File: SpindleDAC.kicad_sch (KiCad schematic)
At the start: 8 parts, among them J13 0-10V Spindle Out, U24 ${SIM.PARAMS}, U25 ${SIM.PARAMS}

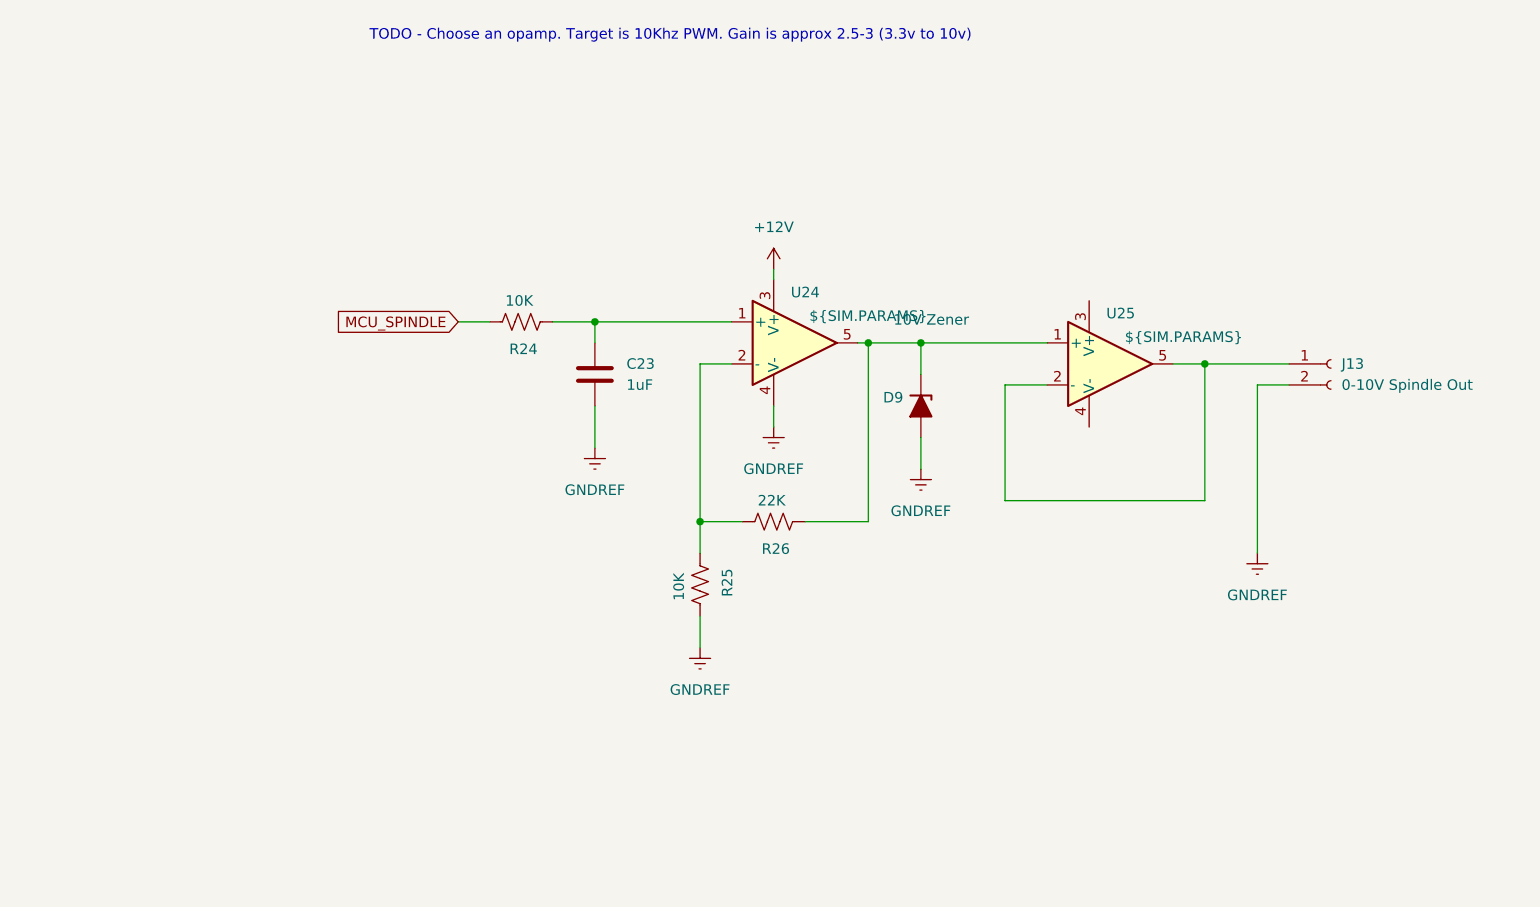
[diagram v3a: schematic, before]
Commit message: restructured power supplies to enable Spindle DAC to be isolated. We now have the option of supplying two 24V inputs, one to power the nucleo and everything logic side and the other to power peripherals. Some testing will be required.
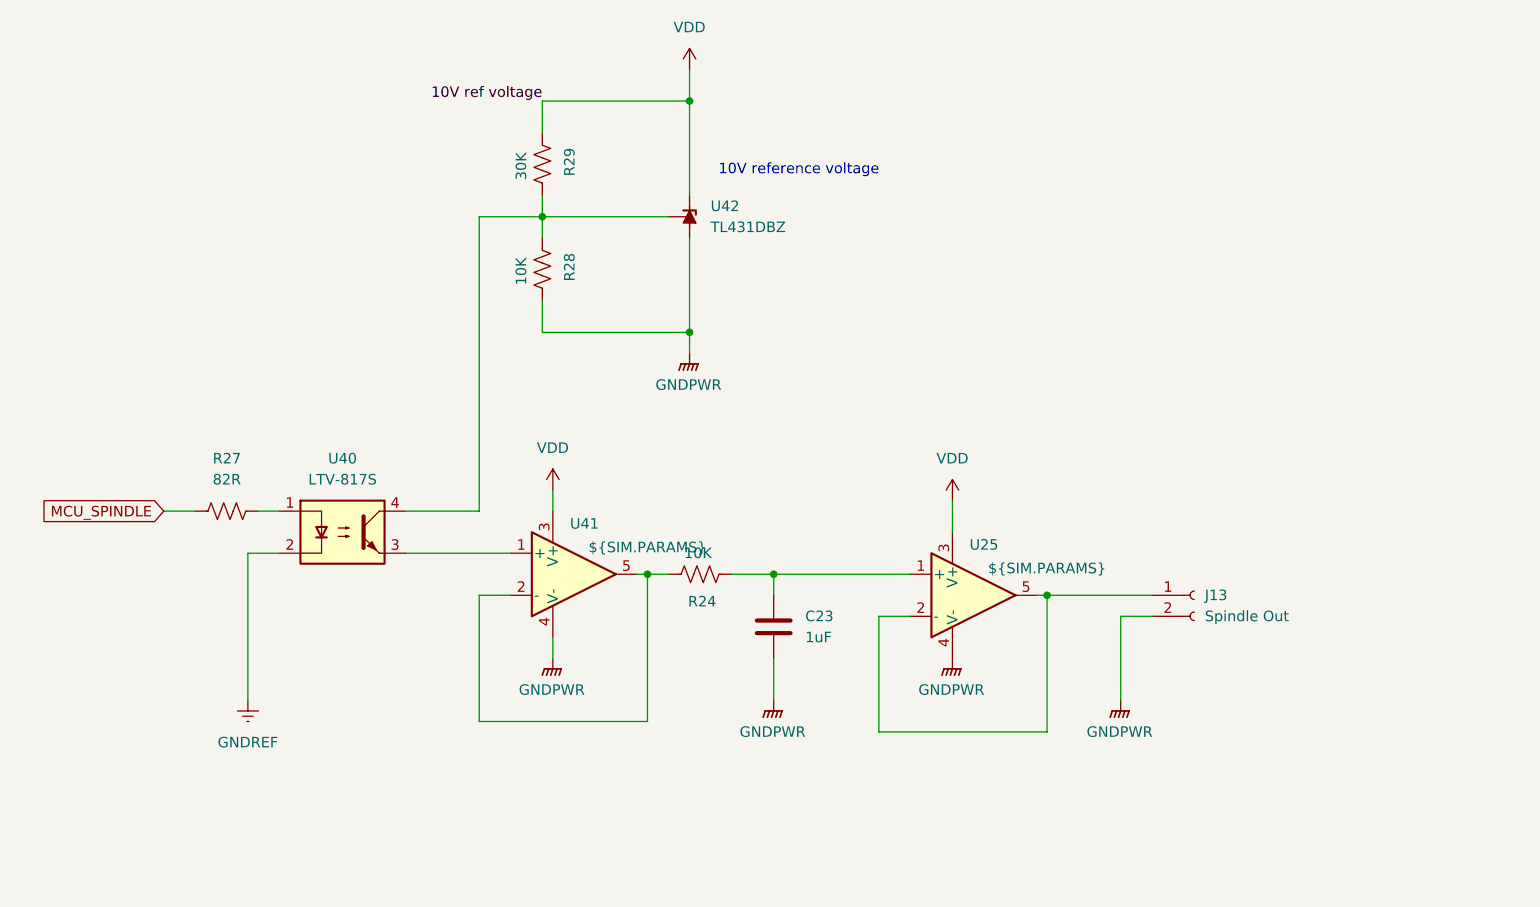
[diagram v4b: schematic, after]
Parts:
- removed D9: 10V Zener, symbol Device:D_Zener_Filled
- removed R25: 10K, symbol Device:R_US
- removed R26: 22K, symbol Device:R_US
- removed U24: ${SIM.PARAMS}, symbol Simulation_SPICE:OPAMP
- added R27: 82R, symbol Device:R_US
- added R28: 10K, symbol Device:R_US
- added R29: 30K, symbol Device:R_US
- added U40: LTV-817S, Package_SO:SOIC-16_3.9x9.9mm_P1.27mm, symbol Isolator:LTV-817S
- added U41: ${SIM.PARAMS}, symbol Simulation_SPICE:OPAMP
- added U42: TL431DBZ, Package_TO_SOT_SMD:SOT-23, symbol Reference_Voltage:TL431DBZ
- J13: value 0-10V Spindle Out -> Spindle Out
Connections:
- net GNDREF: now also U40.2; no longer C23.2, J13.2 (Pin_2)
- net MCU_SPINDLE: now also R27.1; no longer R24.2
- net at U25.1 (+): now also C23.1, R24.1
- net VDD: now reaches U25.3 (V+)
- net VDD: now also R29.1, U41.3 (V+), U42.1 (K)
- net GNDPWR: now reaches U25.4 (V-)
- net GNDPWR: now also C23.2, J13.2 (Pin_2), R28.2, U41.4 (V-), U42.3 (A)
- new net: R28.1, R29.2, U40.4, U42.2 (REF)
- new net: R27.2, U40.1
- new net: U40.3, U41.1 (+)
- new net: R24.2, U41.2 (-), U41.5
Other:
- note added: "10V reference voltage"
- note removed: "TODO - Choose an opamp. Target is 10Khz PWM. Gain is approx 2.5-3 (3.3v to 10v)"
- moved on the sheet: C23, J13, R24, U25

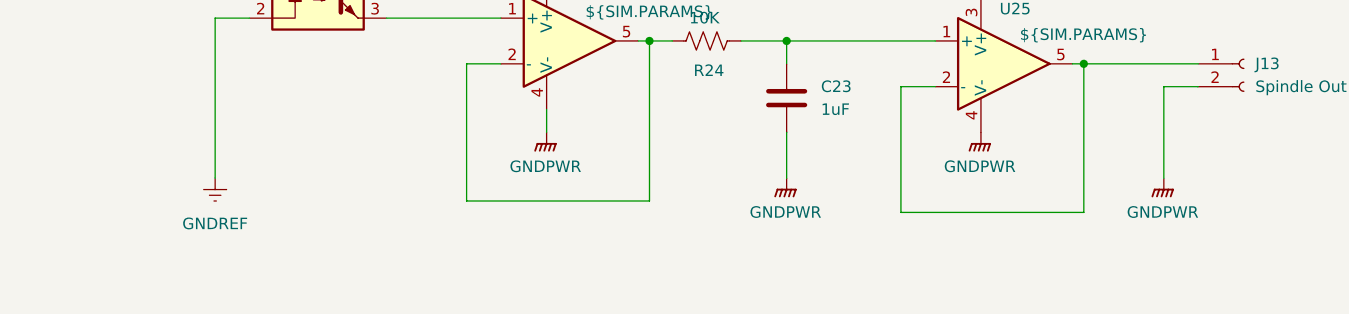
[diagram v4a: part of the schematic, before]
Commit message: Fixes to screw terminal footprints, updated BOM and included in project folder
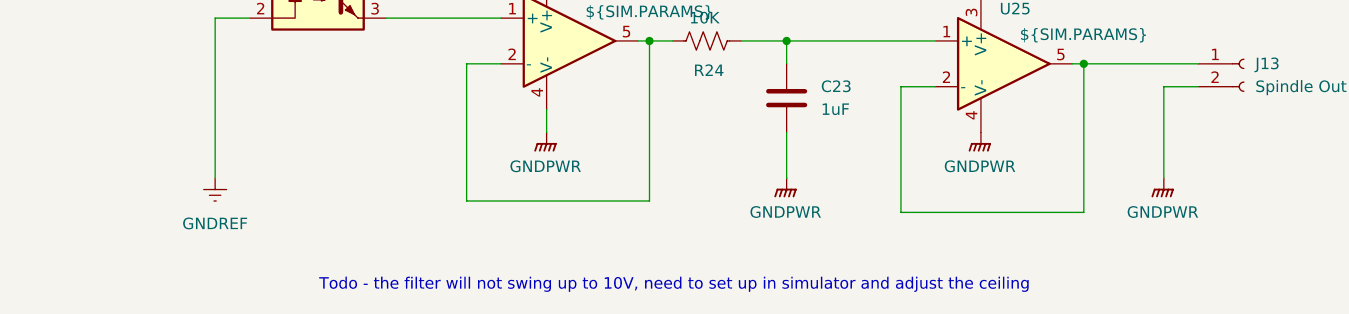
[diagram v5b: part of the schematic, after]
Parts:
- J13: footprint OSTVTerminalBlocks:Conn01x02 -> EBWA_02_A:ADAMTECH_EBWA-02-A
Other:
- note added: "Todo - the filter will not swing up to 10V, need to set up in simulator and adjust the ceiling"
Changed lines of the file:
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@@
+		)
+	)
+	(text "Todo - the filter will not swing up to 10V, need to set up in simulator and adjust the ceiling"
+		(exclude_from_sim no)
+		(at 119.634 128.778 0)
+		(effects
+			(font
+				(size 1.27 1.27)
+			)
 		)
 	)
@@
 			)
 		)
-		(property "Footprint" "OSTVTerminalBlocks:Conn01x02"
+		(property "Footprint" "EBWA_02_A:ADAMTECH_EBWA-02-A"
 			(at 182.88 104.14 0)
 			(effects

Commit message: Fixed bug with lack of pin header for CN11 and CN12. Addeded RPI header and aligned it, assigned some safe footprints
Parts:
- R24, R27, R28, R29: footprint (none) -> Resistor_SMD:R_1206_3216Metric_Pad1.30x1.75mm_HandSolder
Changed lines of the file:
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@@
 			)
 		)
-		(property "Footprint" ""
+		(property "Footprint" "Resistor_SMD:R_1206_3216Metric_Pad1.30x1.75mm_HandSolder"
 			(at 105.156 65.024 90)
 			(effects
@@
 			)
 		)
-		(property "Footprint" ""
+		(property "Footprint" "Resistor_SMD:R_1206_3216Metric_Pad1.30x1.75mm_HandSolder"
 			(at 66.294 92.964 90)
 			(effects
@@
 			)
 		)
-		(property "Footprint" ""
+		(property "Footprint" "Resistor_SMD:R_1206_3216Metric_Pad1.30x1.75mm_HandSolder"
 			(at 105.156 52.324 90)
 			(effects
@@
 			)
 		)
-		(property "Footprint" ""
+		(property "Footprint" "Resistor_SMD:R_1206_3216Metric_Pad1.30x1.75mm_HandSolder"
 			(at 122.936 102.616 90)
 			(effects

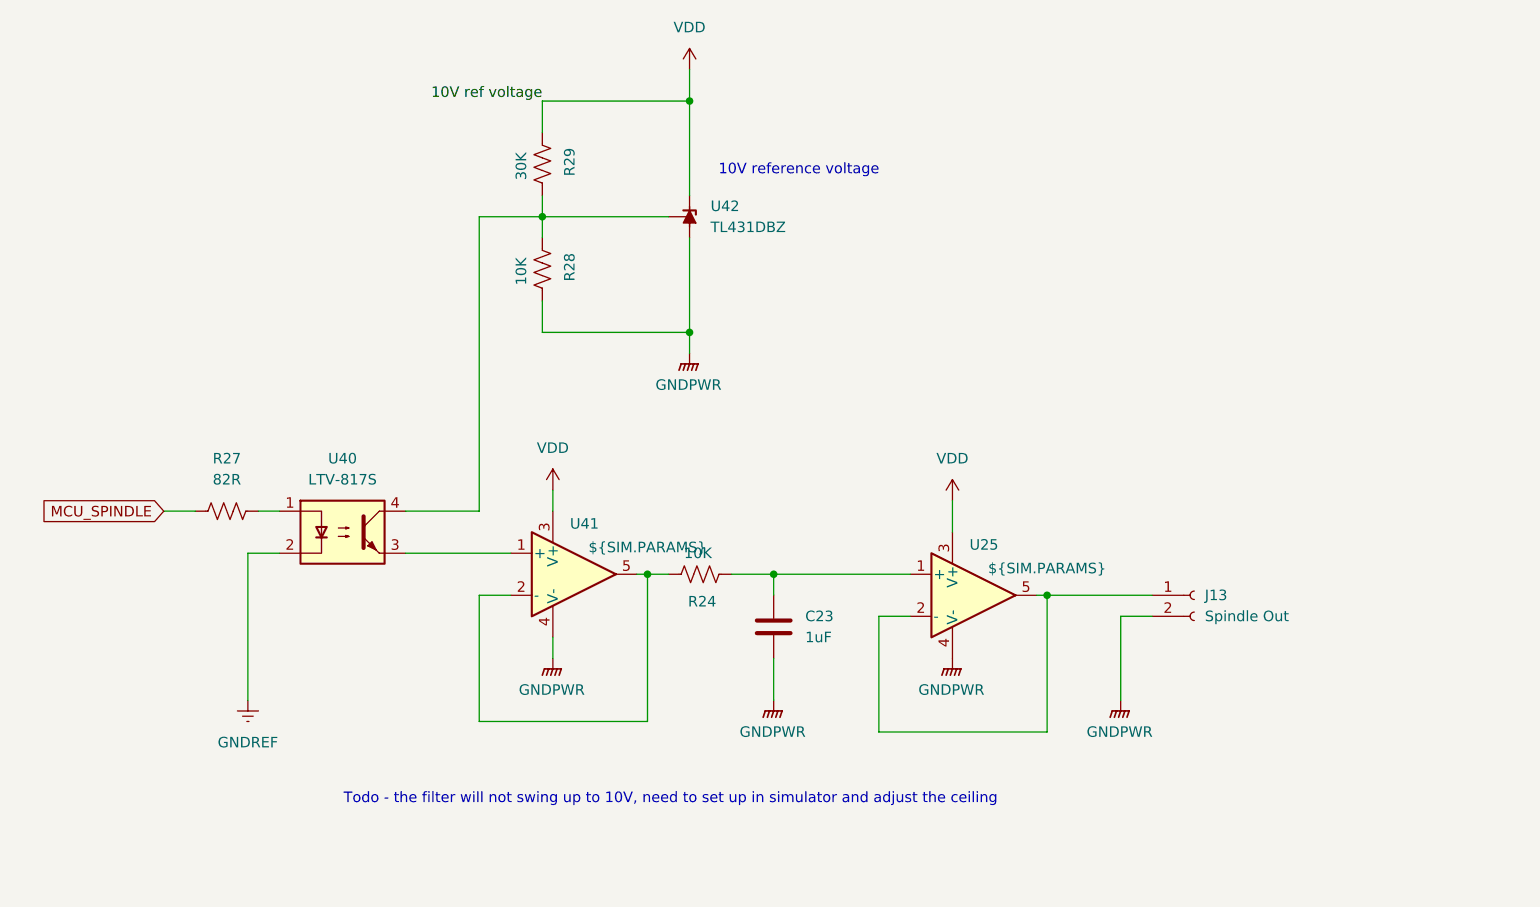
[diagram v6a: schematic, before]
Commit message: updates to read me, marked V1 parts inactive and made start on board layout for initial test board. fixes to BOM to suit
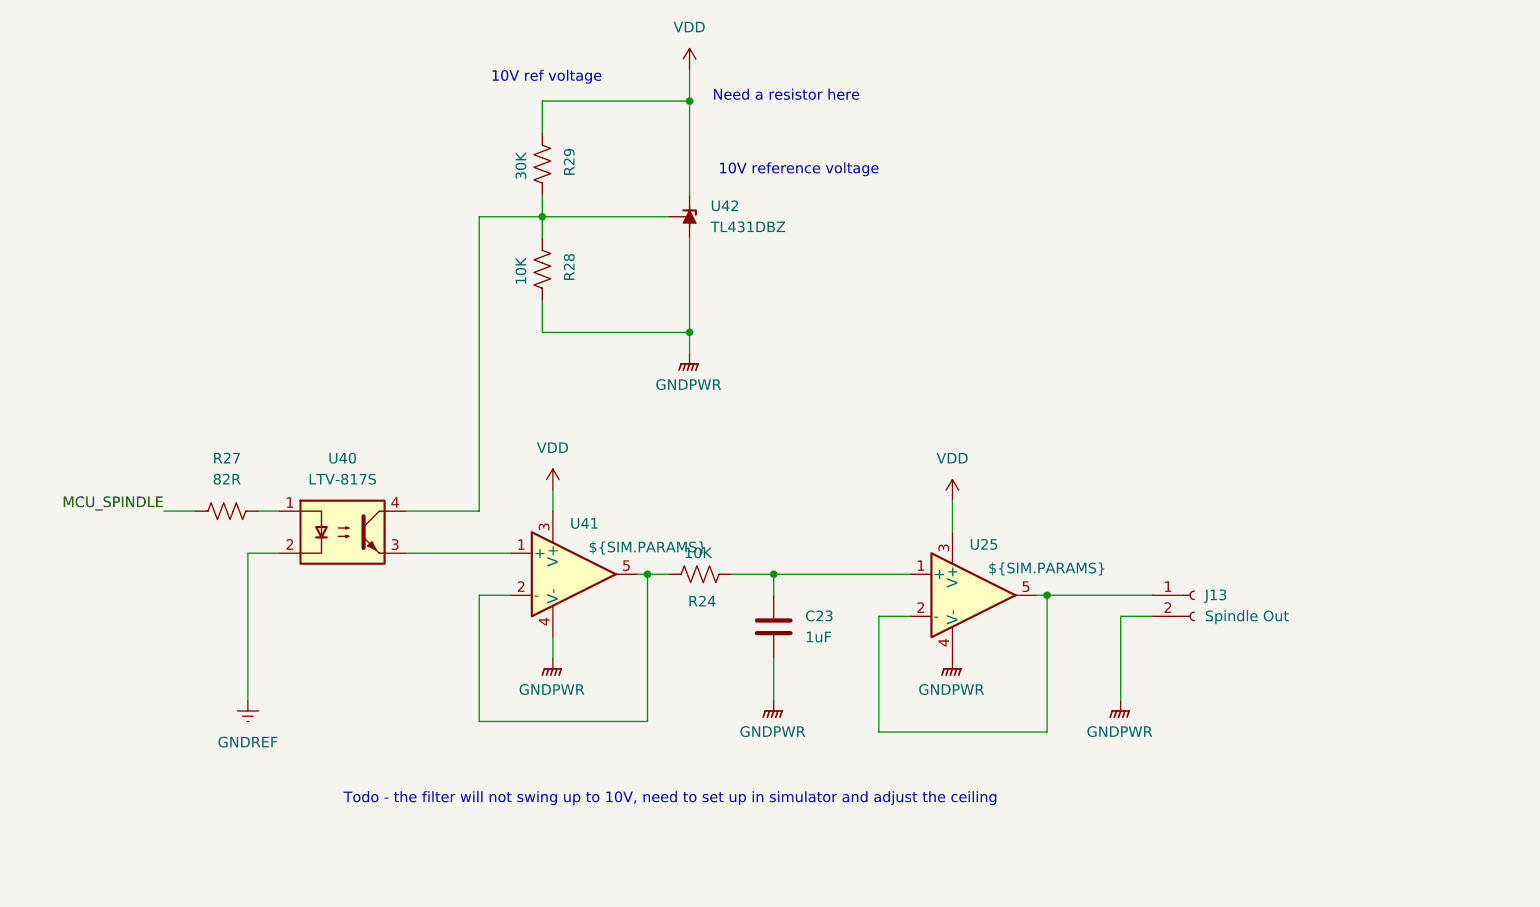
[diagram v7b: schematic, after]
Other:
- note added: "10V ref voltage"
- note added: "Need a resistor here"
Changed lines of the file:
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@@
+		)
+	)
+	(text "Need a resistor here"
+		(exclude_from_sim no)
+		(at 133.604 43.942 0)
+		(effects
+			(font
+				(size 1.27 1.27)
+			)
+		)
+	)
+	(text "10V ref voltage"
+		(exclude_from_sim no)
+		(at 104.648 41.656 0)
+		(effects
+			(font
+				(size 1.27 1.27)
+			)
 		)
 	)
@@
 		)
 	)
-	(label "10V ref voltage"
-		(at 104.14 44.45 180)
+	(label "MCU_SPINDLE"
+		(at 58.42 93.98 180)
 		(effects
 			(font
@@
 		)
 	)
-	(global_label "MCU_SPINDLE"
-		(shape input)
-		(at 58.42 93.98 180)
-		(fields_autoplaced yes)
-		(effects
-			(font
-				(size 1.27 1.27)
-			)
-			(justify right)
-		)
-		(property "Intersheetrefs" "${INTERSHEET_REFS}"
-			(at 43.2076 93.98 0)
-			(effects
-				(font
-					(size 1.27 1.27)
-				)
-				(justify right)
-				(hide yes)
-			)
-		)
-	)
 	(symbol
 		(lib_id "Simulation_SPICE:OPAMP")
@@
 		(exclude_from_sim no)
 		(in_bom yes)
-		(on_board yes)
+		(on_board no)
 		(dnp no)
 		(property "Reference" "U25"
@@
 		(exclude_from_sim no)
 		(in_bom yes)
-		(on_board yes)
+		(on_board no)
 		(dnp no)
 		(property "Reference" "R28"
@@
 		(exclude_from_sim no)
 		(in_bom yes)
-		(on_board yes)
+		(on_board no)
 		(dnp no)
 		(fields_autoplaced yes)
@@
 		(exclude_from_sim no)
 		(in_bom yes)
-		(on_board yes)
+		(on_board no)
 		(dnp no)
 		(fields_autoplaced yes)
@@
 		(exclude_from_sim no)
 		(in_bom yes)
-		(on_board yes)
+		(on_board no)
 		(dnp no)
 		(fields_autoplaced yes)
@@
 		(exclude_from_sim no)
 		(in_bom yes)
-		(on_board yes)
+		(on_board no)
 		(dnp no)
 		(fields_autoplaced yes)
@@
 		(exclude_from_sim no)
 		(in_bom yes)
-		(on_board yes)
+		(on_board no)
 		(dnp no)
 		(fields_autoplaced yes)
@@
 		(exclude_from_sim no)
 		(in_bom yes)
-		(on_board yes)
+		(on_board no)
 		(dnp no)
 		(fields_autoplaced yes)
@@
 		(exclude_from_sim no)
 		(in_bom yes)
-		(on_board yes)
+		(on_board no)
 		(dnp no)
 		(fields_autoplaced yes)
@@
 		(exclude_from_sim no)
 		(in_bom yes)
-		(on_board yes)
+		(on_board no)
 		(dnp no)
 		(fields_autoplaced yes)
@@
 		(exclude_from_sim no)
 		(in_bom yes)
-		(on_board yes)
+		(on_board no)
 		(dnp no)
 		(fields_autoplaced yes)
@@
 		(exclude_from_sim no)
 		(in_bom yes)
-		(on_board yes)
+		(on_board no)
 		(dnp no)
 		(fields_autoplaced yes)
@@
 		(exclude_from_sim no)
 		(in_bom yes)
-		(on_board yes)
+		(on_board no)
 		(dnp no)
 		(property "Reference" "R29"
@@
 		(exclude_from_sim no)
 		(in_bom yes)
-		(on_board yes)
+		(on_board no)
 		(dnp no)
 		(fields_autoplaced yes)
@@
 		(exclude_from_sim no)
 		(in_bom yes)
-		(on_board yes)
+		(on_board no)
 		(dnp no)
 		(property "Reference" "R24"
@@
 		(exclude_from_sim no)
 		(in_bom yes)
-		(on_board yes)
+		(on_board no)
 		(dnp no)
 		(fields_autoplaced yes)
@@
 		(exclude_from_sim no)
 		(in_bom yes)
-		(on_board yes)
+		(on_board no)
 		(dnp no)
 		(fields_autoplaced yes)
@@
 		(exclude_from_sim no)
 		(in_bom yes)
-		(on_board yes)
+		(on_board no)
 		(dnp no)
 		(fields_autoplaced yes)
@@
 		(exclude_from_sim no)
 		(in_bom yes)
-		(on_board yes)
+		(on_board no)
 		(dnp no)
 		(property "Reference" "U41"

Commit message: New optocoupler part choice, removed digikey BOM as have started inputting them into symbol fields. Re-enabled all disabled parts for now and will re-design power supplies soon.
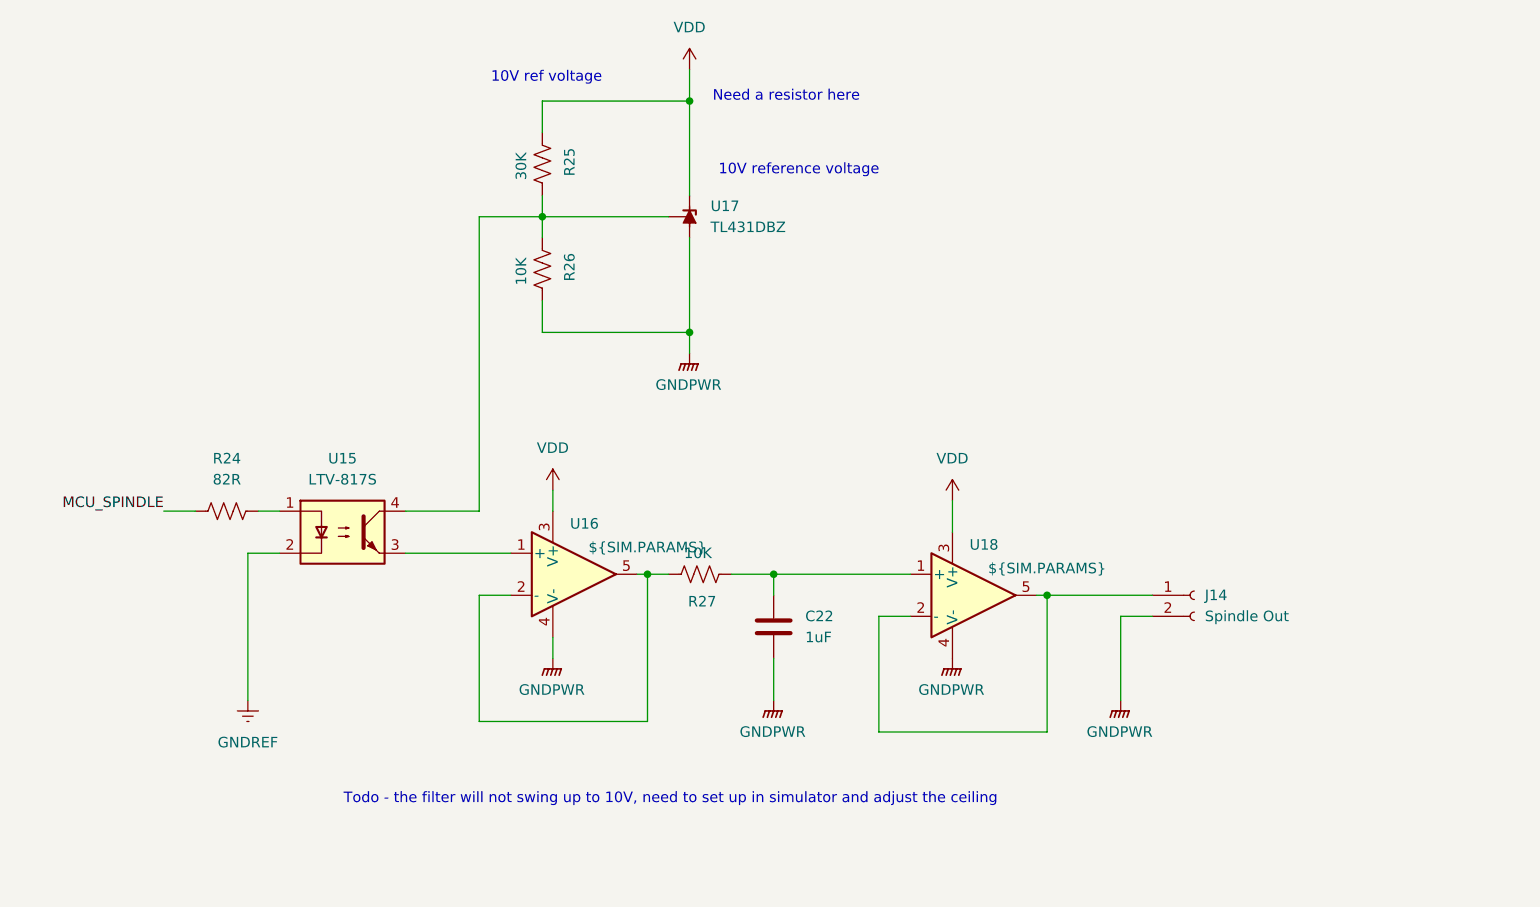
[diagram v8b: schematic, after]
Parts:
- renumbered C23 to C22, J13 to J14, R27 to R24, R29 to R25, R28 to R26, R24 to R27, U40 to U15, U41 to U16, U42 to U17, U25 to U18
